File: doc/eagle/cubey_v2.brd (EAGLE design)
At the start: 80.2 x 61.1 mm, 28 parts, among them K1 PIN20X2

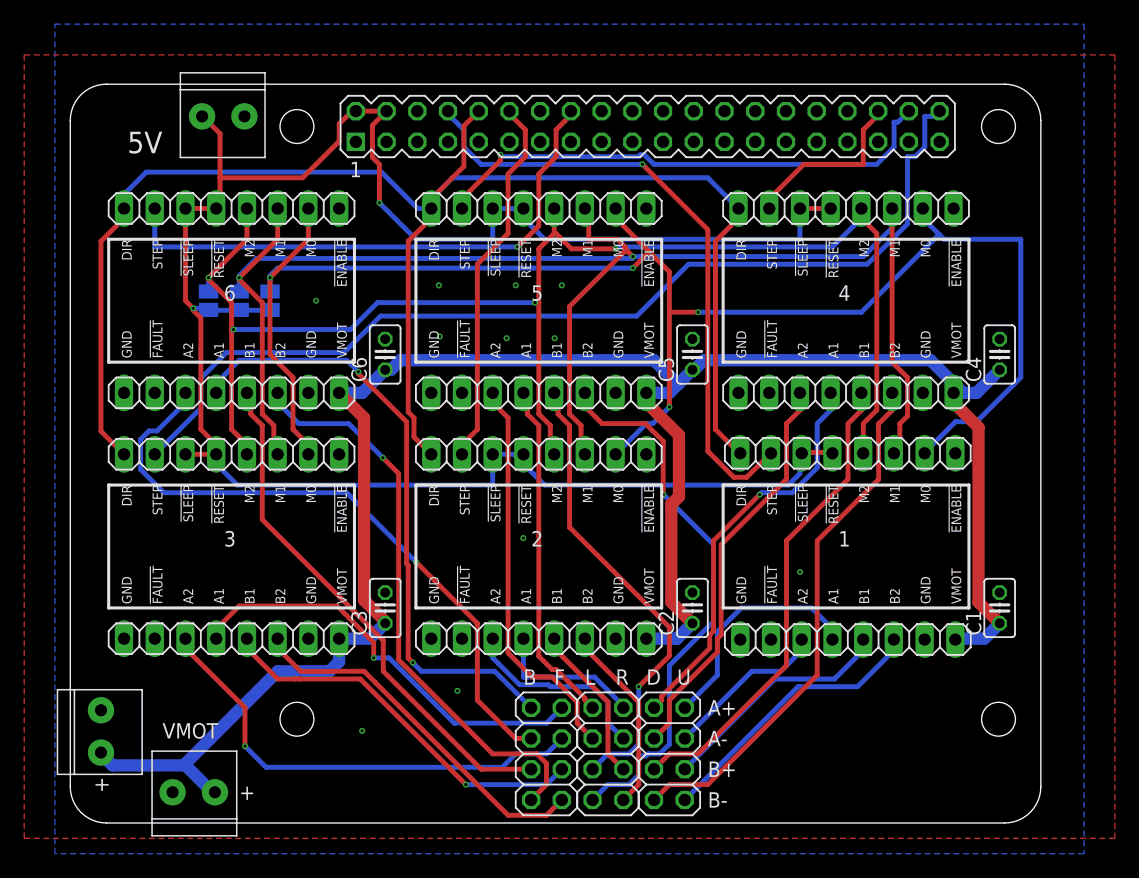
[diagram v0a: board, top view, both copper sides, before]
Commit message: Rename signals in Cubey PCB design. Finalized V2 with ENABLE pin.
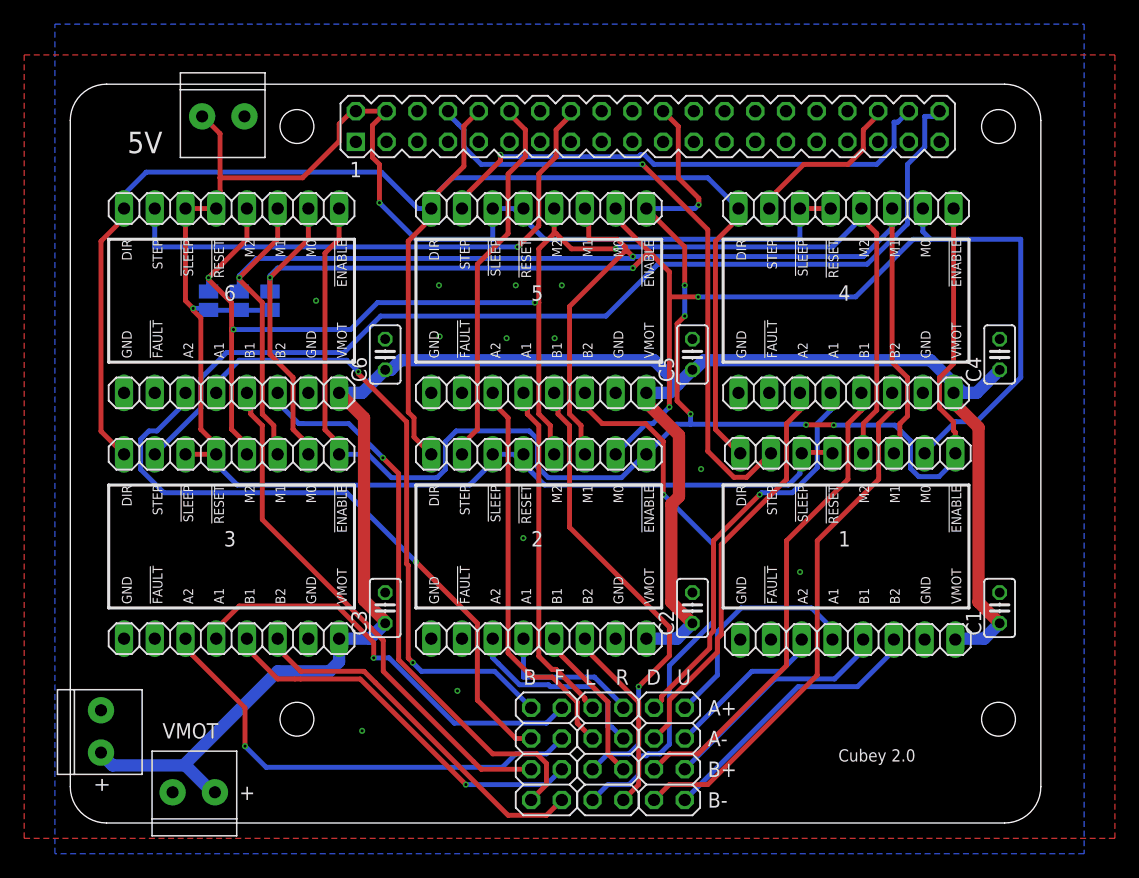
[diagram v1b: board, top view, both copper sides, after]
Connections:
- new net !EN_MOT: JP1.1, JP11.1, JP3.1, JP5.1, JP7.1, JP9.1, K1.22
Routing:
- net !EN_MOT: track 0.00 -> 139.6 mm, vias 0 -> 6
- net +5V: track 171.9 -> 170.8 mm
- net DOWN: track 14.7 -> 13.9 mm
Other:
- board text added: "Cubey 2.0"
